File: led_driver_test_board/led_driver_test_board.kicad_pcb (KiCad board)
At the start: 2 copper layers, 111 parts, among them P1 CONN_01X06_M50-3530642, P2 CONN_01X06_M50-3530642, P3 CONN_01X06_M50-3530642, P4 CONN_01X06_M50-3530642, Q1 Q_NMOS_SSM3K09FULF, Q2 Q_NMOS_SSM3K09FULF, Q3 Q_NMOS_SSM3K09FULF, Q4 Q_NMOS_SSM3K09FULF, Q5 Q_NMOS_SSM3K09FULF, Q6 Q_NMOS_SSM3K09FULF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

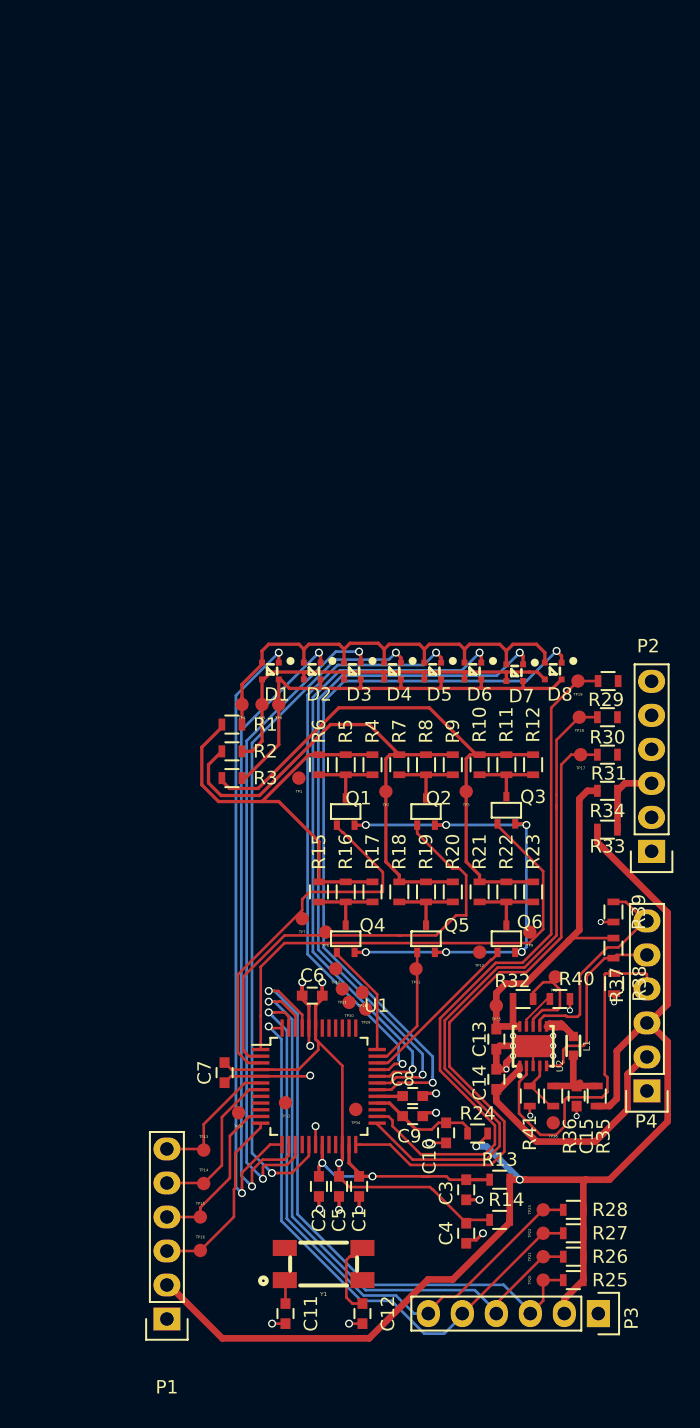
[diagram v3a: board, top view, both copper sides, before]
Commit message: Finished first round of routing, passes DRC
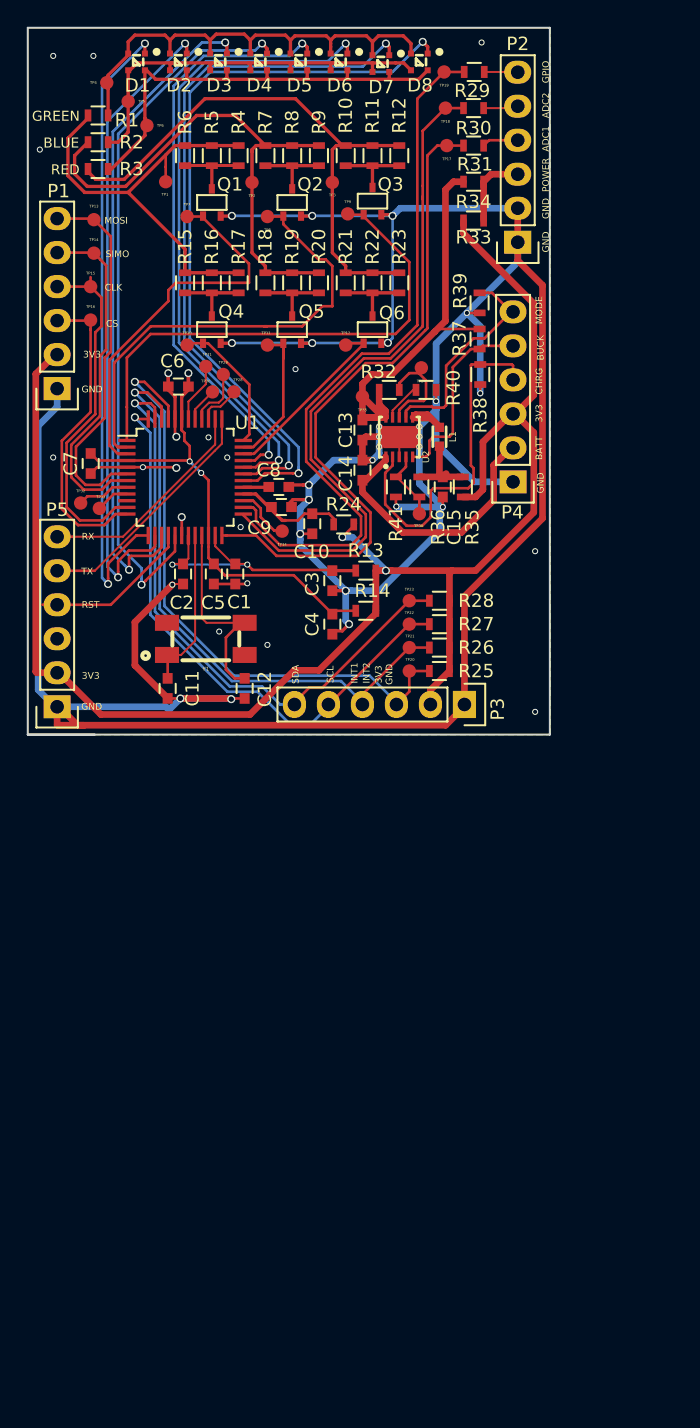
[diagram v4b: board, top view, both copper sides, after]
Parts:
- added P5: CONN_01X06_M50-3530642, Pin_Headers:Pin_Header_Straight_1x06, F.Cu at (102.2, 97.9)
- R10, R21: value SMD-RES-0R-1_4W_0603_ -> CONNEX-SMD-RES-120-0603
- R11, R22: value SMD-RES-0R-1_4W_0603_ -> CONNEX-SMD-RES-60R4-0603
- R12, R23: value SMD-RES-0R-1_4W_0603_ -> CONNEX-SMD-RES-40R2-0603
- R15, R4: value SMD-RES-0R-1_4W_0603_ -> CONNEX-SMD-RES-20-0603
- R16, R20, R5, R9: value SMD-RES-0R-1_4W_0603_ -> CONNEX-SMD-RES-10-0603
- R17, R6: value SMD-RES-0R-1_4W_0603_ -> CONNEX-SMD-RES-6R65-0603
- R18, R7: value SMD-RES-0R-1_4W_0603_ -> CONNEX-SMD-RES-30-0603
- R19, R8: value SMD-RES-0R-1_4W_0603_ -> CONNEX-SMD-RES-15-0603
- R40: value CONNEX-SMD-RES-0-0603 -> CONNEX-SMD-RES-4K02-0603
- moved P1 70.0 mm to (102.2, 74.2)
- moved TP13 70.0 mm to (104.9, 61.5)
- moved TP14 70.0 mm to (104.9, 64.0)
- moved TP15 70.0 mm to (104.7, 66.5)
- moved TP16 70.0 mm to (104.7, 69.0)
- moved TP9 55.3 mm to (123.9, 61.1)
- moved TP8 53.6 mm to (117.9, 61.3)
- moved TP7 53.2 mm to (111.9, 61.3)
- moved TP29 48.6 mm to (114.6, 73.1)
- moved TP10 47.9 mm to (111.9, 70.9)
- moved TP11 47.9 mm to (117.9, 70.9)
- moved TP31 47.6 mm to (113.3, 72.5)
- moved TP4 47.5 mm to (105.9, 51.3)
- moved Y1 47.5 mm to (113.3, 92.8)
- moved C11 47.5 mm to (110.5, 96.5)
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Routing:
- net GND: track 82.8 -> 298.7 mm
- net +3V3: track 98.1 -> 128.7 mm
- net /BOOT_TX: track 0.00 -> 19.5 mm
- net /SPI_MOSI: track 10.2 -> 27.9 mm
- net /BOOT_RX: track 0.00 -> 16.7 mm
- net /SPI_CLK: track 12.4 -> 26.4 mm
- net /SPI_SIMO: track 12.4 -> 26.0 mm
- net /RESET_N: track 0.00 -> 12.1 mm
- net Net-(C11-Pad1): track 1.77 -> 12.2 mm
- net Net-(C12-Pad1): track 5.76 -> 15.4 mm
- net /SPI_CS: track 13.9 -> 23.2 mm
- net /3V3_CHARGE_INPUT: track 29.0 -> 35.6 mm
- net /LED_DRV_BLUE: track 39.3 -> 45.6 mm
- net /LED_DRV_RED: track 42.4 -> 48.3 mm
- net /LED_DRV_GREEN: track 32.3 -> 37.2 mm
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- added copper zone on B.Cu, net GND
- added copper zone on F.Cu, net GND
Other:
- board outline added: 39 x 52.8 mm
- board text added: "3V3"
- board text added: "ADC1"
- board text added: "ADC2"
- board text added: "BATT"
- board text added: "BLUE"
- board text added: "BUCK"
- board text added: "CHRG"
- board text added: "CLK"
- board text added: "CS"
- board text added: "GND"
- board text added: "GPIO"
- board text added: "GREEN"
- board text added: "INT1"
- board text added: "INT2"
- board text added: "MODE"
- board text added: "MOSI"
- board text added: "POWER"
- board text added: "RED"
- board text added: "RST"
- board text added: "RX"
- board text added: "SCL"
- board text added: "SDA"
- board text added: "SIMO"
- board text added: "TX"

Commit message: Replaced R35 with correct BOM
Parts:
- R35: value CONNEX-SMD-RES-0-0603 -> SMD-RES-0R-1_4W_0603_
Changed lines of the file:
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@@
   )
   (setup
-    (last_trace_width 0.2)
+    (last_trace_width 0.152)
     (user_trace_width 0.2)
     (user_trace_width 0.25)
@@
       (effects (font (size 1 1) (thickness 0.15)))
     )
-    (fp_text value CONNEX-SMD-RES-0-0603 (at 0 1.9 270) (layer F.Fab)
+    (fp_text value SMD-RES-0R-1_4W_0603_ (at 0 1.9 270) (layer F.Fab)
       (effects (font (size 1 1) (thickness 0.15)))
     )
@@
     (effects (font (size 0.5 0.5) (thickness 0.125)))
   )
-  (gr_text GND (at 104.77381 97.9 360) (layer F.SilkS)
+  (gr_text GND (at 104.77381 97.9) (layer F.SilkS)
     (effects (font (size 0.5 0.5) (thickness 0.125)))
   )
@@
     (effects (font (size 0.5 0.5) (thickness 0.125)))
   )
-  (gr_text GND (at 104.8 74.2 360) (layer F.SilkS)
+  (gr_text GND (at 104.8 74.2) (layer F.SilkS)
     (effects (font (size 0.5 0.5) (thickness 0.125)))
   )

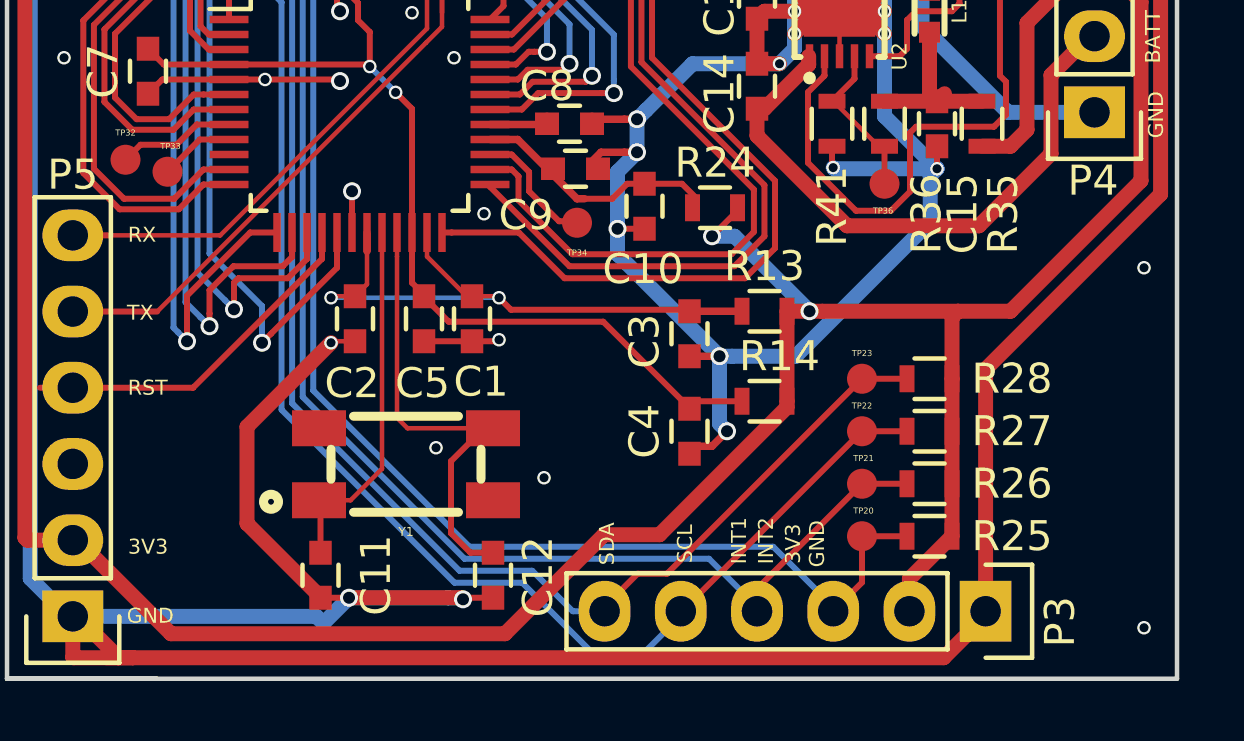
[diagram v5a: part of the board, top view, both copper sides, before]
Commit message: Added logo and rev info to silkscreen
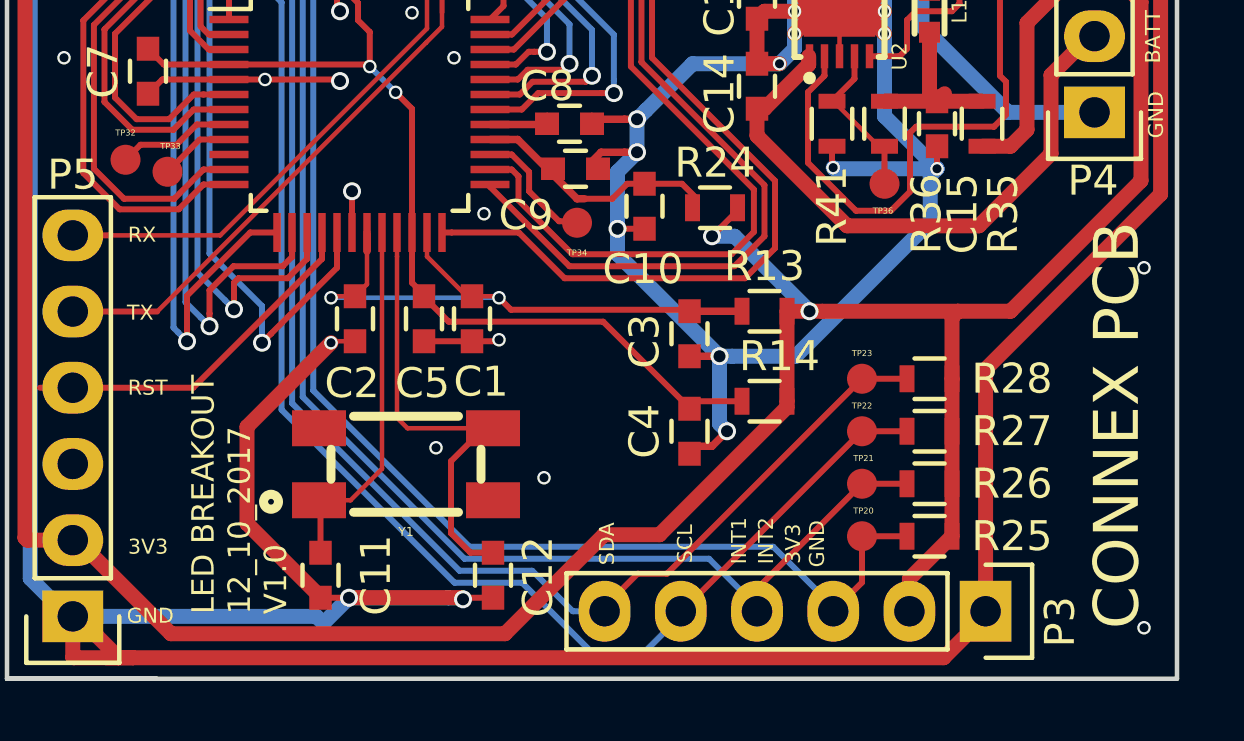
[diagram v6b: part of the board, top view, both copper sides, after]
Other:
- board text added: "CONNEX PCB"
- board text added: "LED BREAKOUT 12_10_2017 V1.0"
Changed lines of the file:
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@@
     (area 99.924999 47.124999 139.075001 100.075001)
     (thickness 1.6)
-    (drawings 37)
+    (drawings 39)
     (tracks 970)
     (zones 0)
@@
     )
   )
+  (gr_text "LED BREAKOUT\n12_10_2017\nV1.0" (at 107.75 97.85 90) (layer F.SilkS)
+    (effects (font (size 0.75 0.75) (thickness 0.1875)) (justify left))
+  )
+  (gr_text "CONNEX PCB" (at 137 91.55 90) (layer F.SilkS)
+    (effects (font (size 1.5 1.5) (thickness 0.3)))
+  )
   (gr_text GREEN (at 102.1 53.8) (layer F.SilkS)

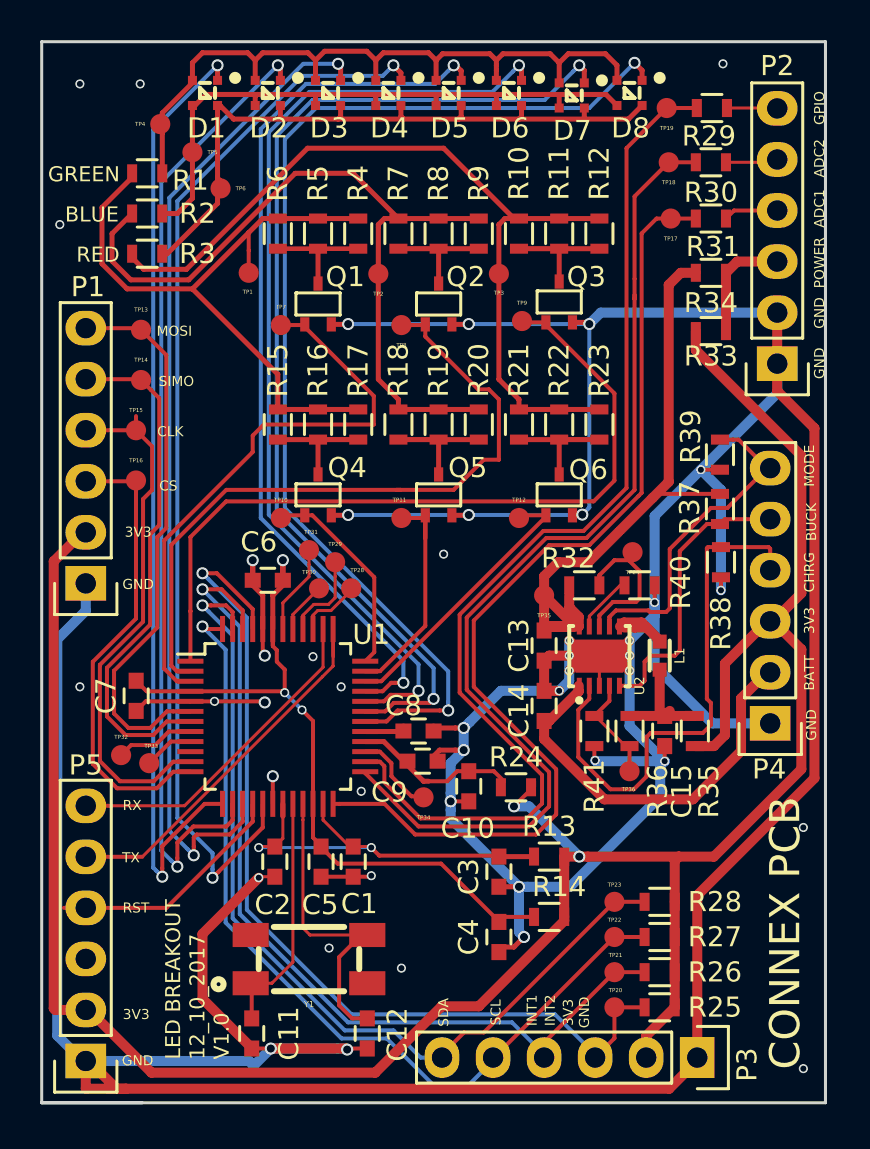
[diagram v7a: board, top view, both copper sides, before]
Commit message: Version 1.1 - Unreveiwed - updated footprints for leds, crystal regulator, general layout, font sizes for labels
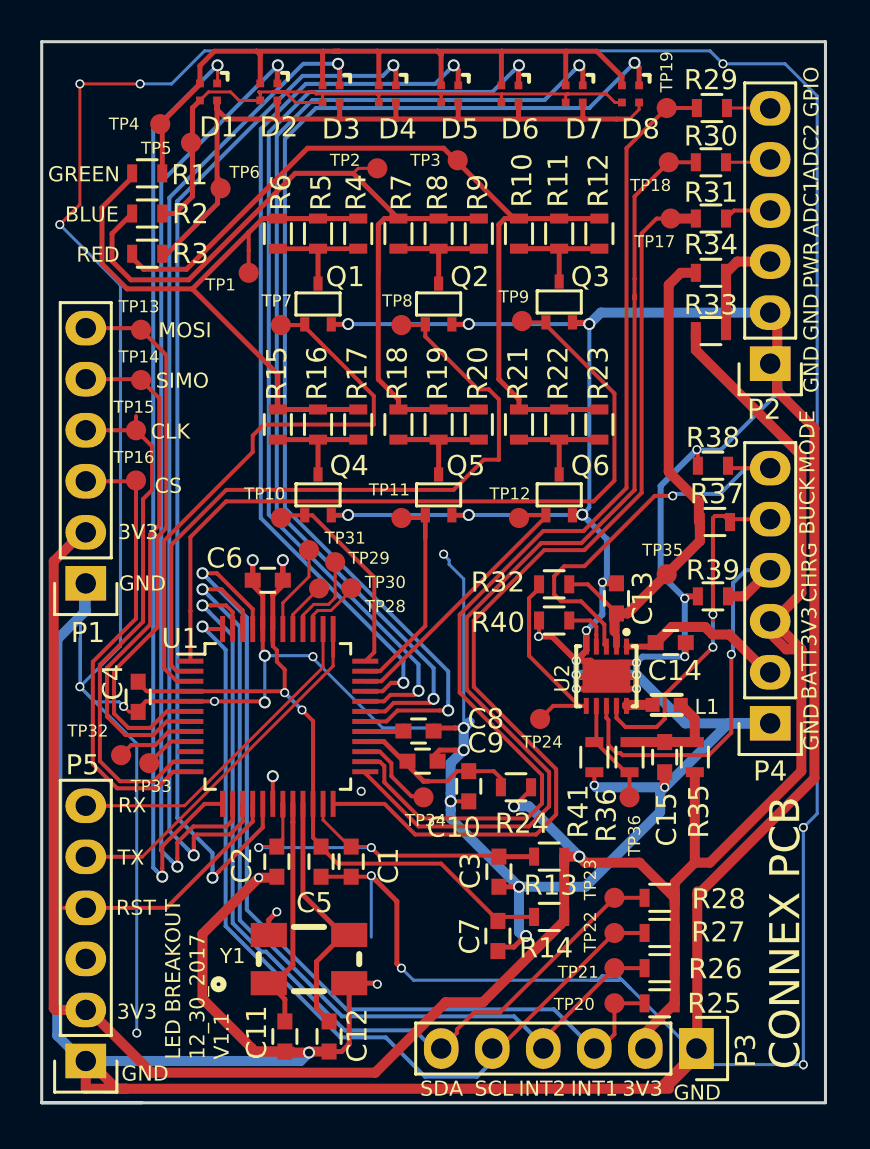
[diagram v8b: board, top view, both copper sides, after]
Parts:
- added G***111111: LOGO, connex_logos:chicken_outline_12mmx15mm, B.Cu at (129.1, 53.3)
- added G***111111: LOGO, connex_logos:chicken_outline_12mmx15mm, B.Cu at (118.3, 53.3)
- added G***111111: LOGO, connex_logos:chicken_outline_12mmx15mm, B.Cu at (107.5, 53.3)
- added G***111112: LOGO, connex_logos:chicken_outline_12mmx15mm, B.Cu at (129.1, 65.3)
- added G***111112: LOGO, connex_logos:chicken_outline_12mmx15mm, B.Cu at (118.3, 65.3)
- added G***111112: LOGO, connex_logos:chicken_outline_12mmx15mm, B.Cu at (107.5, 65.3)
- added G***111113: LOGO, connex_logos:chicken_outline_12mmx15mm, B.Cu at (129.1, 77.3)
- added G***111113: LOGO, connex_logos:chicken_outline_12mmx15mm, B.Cu at (118.3, 77.3)
- added G***111113: LOGO, connex_logos:chicken_outline_12mmx15mm, B.Cu at (107.5, 77.3)
- added G***111114: LOGO, connex_logos:chicken_outline_12mmx15mm, B.Cu at (129.1, 89.3)
- added G***111114: LOGO, connex_logos:chicken_outline_12mmx15mm, B.Cu at (118.3, 89.3)
- added G***111114: LOGO, connex_logos:chicken_outline_12mmx15mm, B.Cu at (107.5, 89.3)
- C1, C2: value connex_cap_100NF_0603_10V -> CONNEX-SMD-CAP-10NF-0603
- moved C7 21.6 mm to (122.7, 91.7)
- moved C4 21.6 mm to (104.8, 79.8)
- moved TP24 9.49 mm to (124.8, 80.9)
- moved R39 7.06 mm to (133.4, 74.8), turned to 180 degrees
- moved C14 7.04 mm to (131.3, 77.1), turned to 180 degrees
- moved TP35 6.19 mm to (131.1, 73.7)
- moved TP3 6.01 mm to (120.7, 53.1)
- moved TP2 5.25 mm to (116.7, 53.5)
- moved R38 4.82 mm to (133.4, 68.3), turned to 180 degrees
- moved R40 4.60 mm to (125.5, 76.0), turned to 0 degrees
- moved C13 4.30 mm to (128.6, 74.9), turned to 90 degrees
- moved L1 2.47 mm to (131.1, 80.2), turned to 0 degrees
- moved C12 1.91 mm to (114.3, 96.7)
- moved C11 1.66 mm to (112.1, 96.7)
- moved R32 1.50 mm to (125.5, 74.2), turned to 0 degrees
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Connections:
- P4 pad 4: /EN_CHRG -> /MODE
- P4 pad 6: /MODE -> /EN_CHRG
- Y1 pad 2: (no net) -> GND
- Y1 pad 4: (no net) -> GND
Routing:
- net GND: track 298.7 -> 514.6 mm, vias 32 -> 47
- net /BATT_CONN_OUTPUT: track 20.2 -> 8.49 mm
- net /3V3_CHARGE_INPUT: track 35.6 -> 27.1 mm
- net /EN_CHRG: track 27.4 -> 20.3 mm, vias 0 -> 1
- net /MODE: track 16.5 -> 21.0 mm, vias 0 -> 1
- net /EN_BUCK: track 14.4 -> 17.6 mm, vias 0 -> 2
- net /LED_RED: track 35.1 -> 38.1 mm
- net Net-(R32-Pad1): track 7.30 -> 10.2 mm
- net Net-(C12-Pad1): track 15.4 -> 12.8 mm
- net Net-(L1-Pad1): track 3.60 -> 1.31 mm
- net /LED_GREEN: track 36.4 -> 38.6 mm
- net /LED_DRV_BLUE: track 45.6 -> 46.9 mm
- net /REG_OUTPUT_3V3: track 5.65 -> 6.89 mm
- net +3V3: track 128.7 -> 127.5 mm
- net /LED_DRV_RED: track 48.3 -> 49.2 mm
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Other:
- board text added: "LED BREAKOUT 12_30_2017 V1.1"
- board text added: "PWR"
- board text removed: "LED BREAKOUT 12_10_2017 V1.0"
- board text removed: "POWER"
